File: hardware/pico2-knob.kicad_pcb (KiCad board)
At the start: 2 copper layers, 80 x 80 mm, 9 parts, among them J1 OLED_0.87_I2C, J2 LiPo_JST_PH, SW1 SW_Push, SW2 SW_Push, SW3 SW_Push, U1 nice!nano_v2

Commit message: Center button arc, offset OLED header, add nano standoff + OLED 3D model
- Buttons: SW_PUSH_6mm origin is its top-left pad (+3.25mm X from body
  center); shift origins so the visible arc is symmetric about the centerline.
- OLED header J1 moved ~18mm left so the plugged-in module's glass centers
  over the knob (per the module MCAD drawing).
- nano 3D model dropped 8.5mm onto its sockets (clears the encoder peg).
- Attach oled.step to J1 as a 3D model (glass-centering check in KiCad 3D).
All re-routed, DRC clean.

Co-Authored-By: Claude Opus 4.8 <noreply@anthropic.com>
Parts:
- moved J1 18.0 mm to (132.0, 73.0)
- moved SW1 3.25 mm to (129.8, 113.0)
- moved SW2 3.25 mm to (146.8, 120.0)
- moved SW3 3.25 mm to (163.8, 113.0)
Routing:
- net BTN2: track 47.8 -> 6.50 mm
- net BTN3: track 37.7 -> 6.50 mm
- net SDA: track 64.7 -> 86.2 mm
- net VBAT: track 87.7 -> 74.5 mm
- net SCL: track 77.0 -> 78.9 mm
- net BTN1: track 55.0 -> 53.8 mm
- net +3V3: track 96.9 -> 97.7 mm

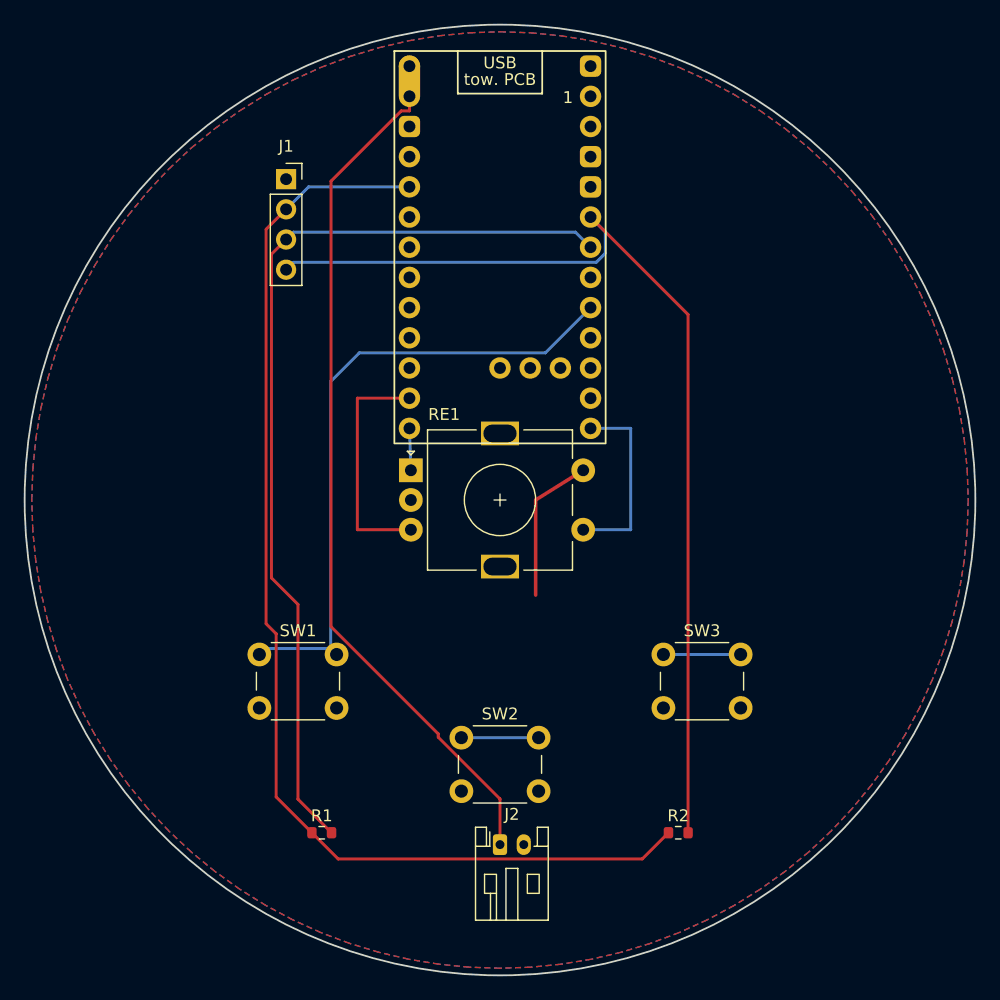
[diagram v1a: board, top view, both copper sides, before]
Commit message: Finalize PCB: trimmed outline, lowered encoder, 4x M3 mounting holes
- Outline shrunk to a Ø74 vertical lens (flat left/right trims, empty space).
- Encoder lowered 8mm; nano nudged down to clear the smaller top rim.
- 4x M3 NPTH mounting holes (board-only): 3 corners + an inset top-left.
- Includes hand-routing/placement (R1/R2/J2 moves, VBAT @0.4mm, the 3 manual
  ratsnest routes) done in the GUI. Ratsnest 0, DRC 0 violations.

NOTE: board is hand-finalized past gen_pcb.py (scaffold only now) -- the .kicad_pcb
is the source of truth; do not re-run gen_pcb or manual routing/moves are lost.

Co-Authored-By: Claude Opus 4.8 <noreply@anthropic.com>
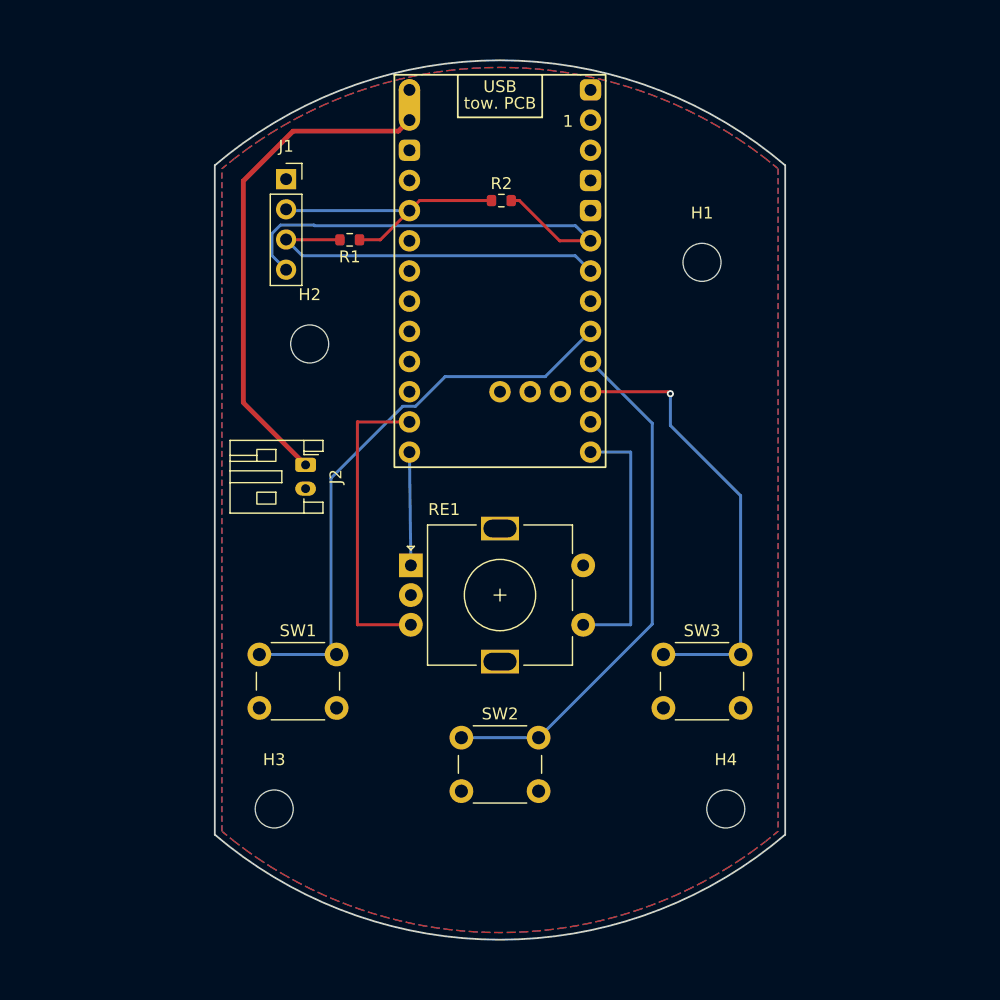
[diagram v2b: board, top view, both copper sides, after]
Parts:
- added H1: MountingHole_3.2mm_M3, MountingHole_3.2mm_M3, F.Cu at (167.0, 80.0)
- added H2: MountingHole_3.2mm_M3, MountingHole_3.2mm_M3, F.Cu at (134.0, 86.9)
- added H3: MountingHole_3.2mm_M3, MountingHole_3.2mm_M3, F.Cu at (131.0, 126.0)
- added H4: MountingHole_3.2mm_M3, MountingHole_3.2mm_M3, F.Cu at (169.0, 126.0)
- moved R2 55.2 mm to (150.1, 74.8)
- moved R1 50.0 mm to (137.4, 78.1), turned to 180 degrees
- moved J2 35.9 mm to (133.6, 97.0), turned to -90 degrees
- moved RE1 8.00 mm to (142.5, 105.5)
- moved U1 2.00 mm to (150.0, 82.0)
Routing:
- net +3V3: track 97.7 -> 22.9 mm
- net SCL: track 78.9 -> 31.3 mm
- net SDA: track 86.2 -> 39.3 mm
- net BTN2: track 6.50 -> 44.3 mm
- net BTN3: track 6.50 -> 37.7 mm, vias 0 -> 1
- net VBAT: track 74.5 -> 44.7 mm
- net GND: track 12.7 -> 0.00 mm
- net ENC_SW: track 15.9 -> 21.9 mm
- net ENC_B: track 19.9 -> 25.9 mm
- net ENC_A: track 3.53 -> 9.53 mm
- net BTN1: track 53.8 -> 48.3 mm
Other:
- board size 80 x 80 mm -> 48 x 74 mm
